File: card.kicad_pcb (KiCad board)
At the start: 2 copper layers, 90 x 50 mm, 8 parts

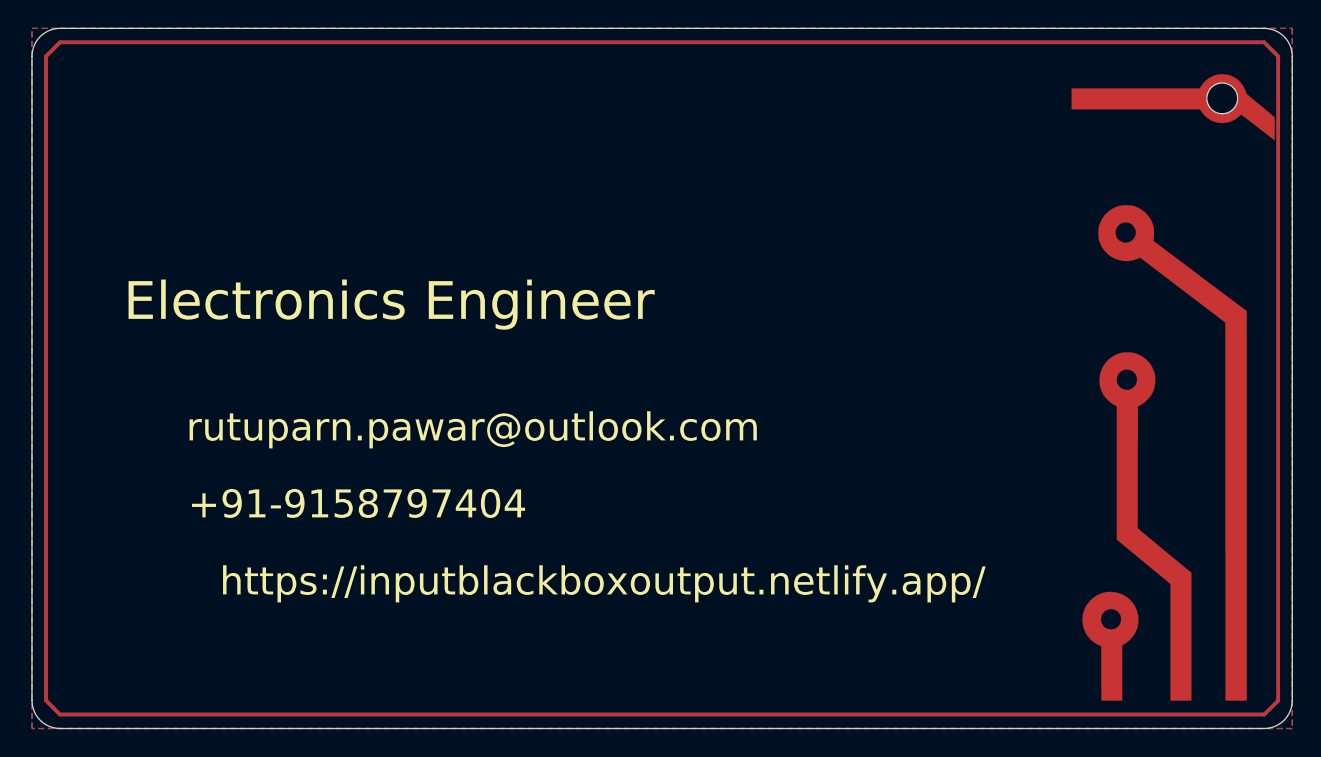
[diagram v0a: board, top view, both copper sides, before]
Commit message: Markings added
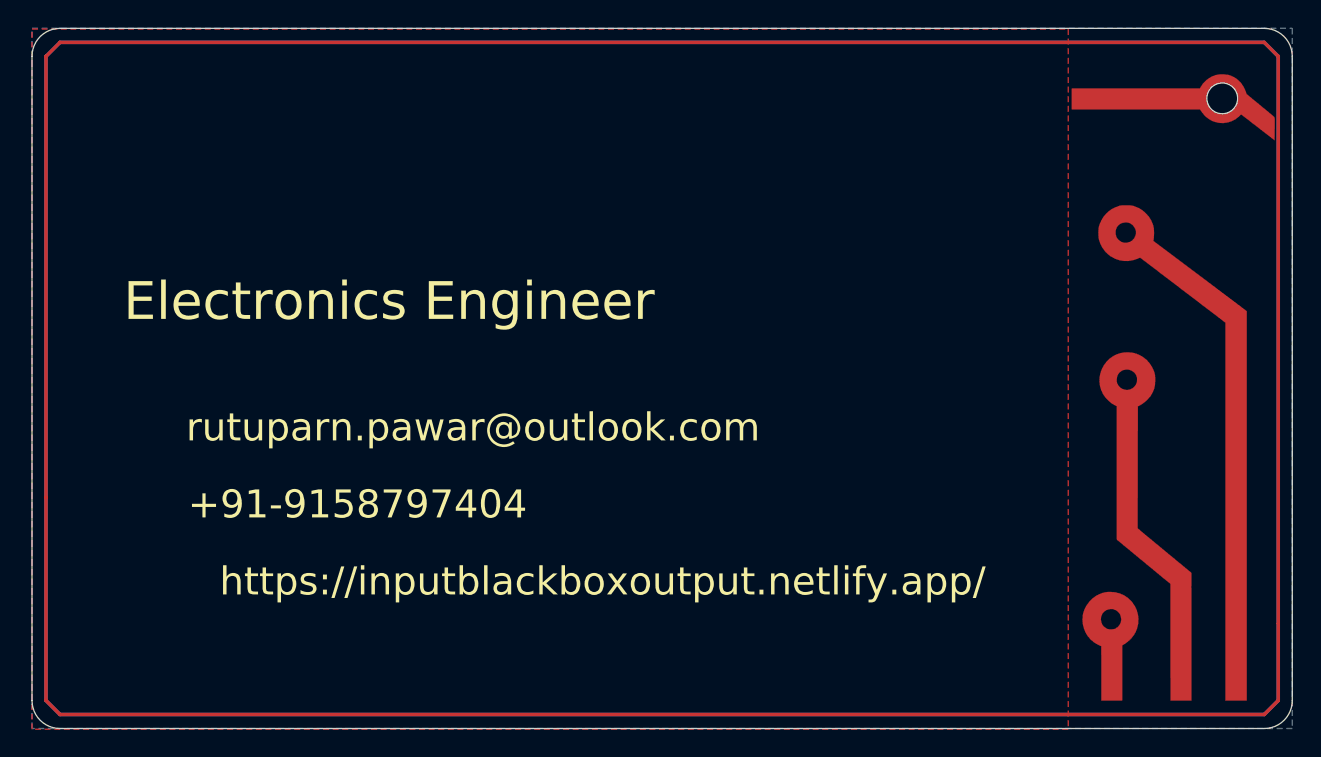
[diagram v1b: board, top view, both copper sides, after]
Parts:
- added REF**: WEEE-Logo_4.2x6mm_SilkScreen, Artwork:WEEE-Logo-SilkScreen, B.Cu at (166.8, 116.2)
- added REF**: OSHW-Symbol_6.7x6mm_SilkScreen, Artwork:OSHW-Symbol-SilkScreen, B.Cu at (169.3, 116.2)
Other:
- board text added: "InputBlackBoxOutput"

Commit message: Update phone number
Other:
- board text added: "+1 737-298-7403"
- board text removed: "+91-9158797404"
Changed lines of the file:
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@@
     (effects (font (size 2.7 2.7) (thickness 0.27)))
   )
-  (gr_text +91-9158797404 (at 123.25 103.75) (layer F.SilkS)
+  (gr_text "+1 737-298-7403" (at 124.5 103.75) (layer F.SilkS)
     (effects (font (size 2 2) (thickness 0.2)))
   )

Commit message: Computer Engineer
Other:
- board text added: "Computer Engineer"
- board text removed: "Electronics Engineer"
